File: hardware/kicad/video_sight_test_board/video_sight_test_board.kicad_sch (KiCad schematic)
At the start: 52 parts, among them J1 BATTERY, J2 XIAO_BREAKOUT_BOARD, J3 LCD, J4 BNO055_MODULE, J4 Conn_01x03_Pin, J5 ATtiny1616_LEFT, J6 ATtiny1616_RIGHT, J7 INPUT_DEVICE, Q1 AO3401A, SW1 SW_BATT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

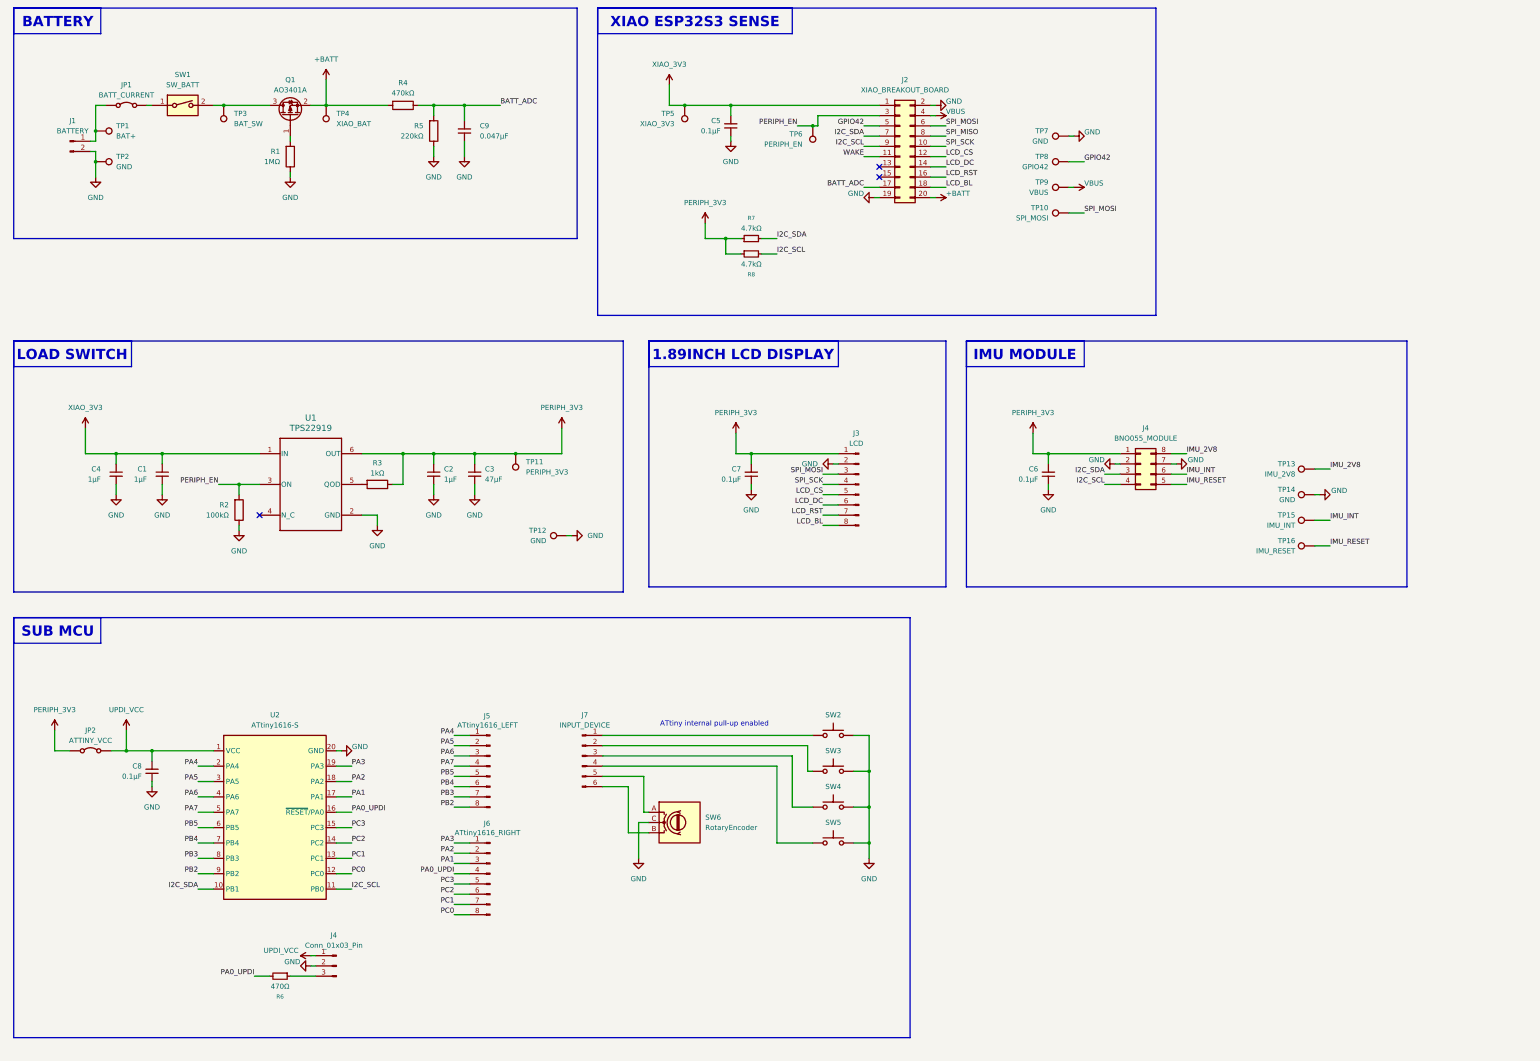
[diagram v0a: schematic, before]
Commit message: I2Cプルアップ注記追加
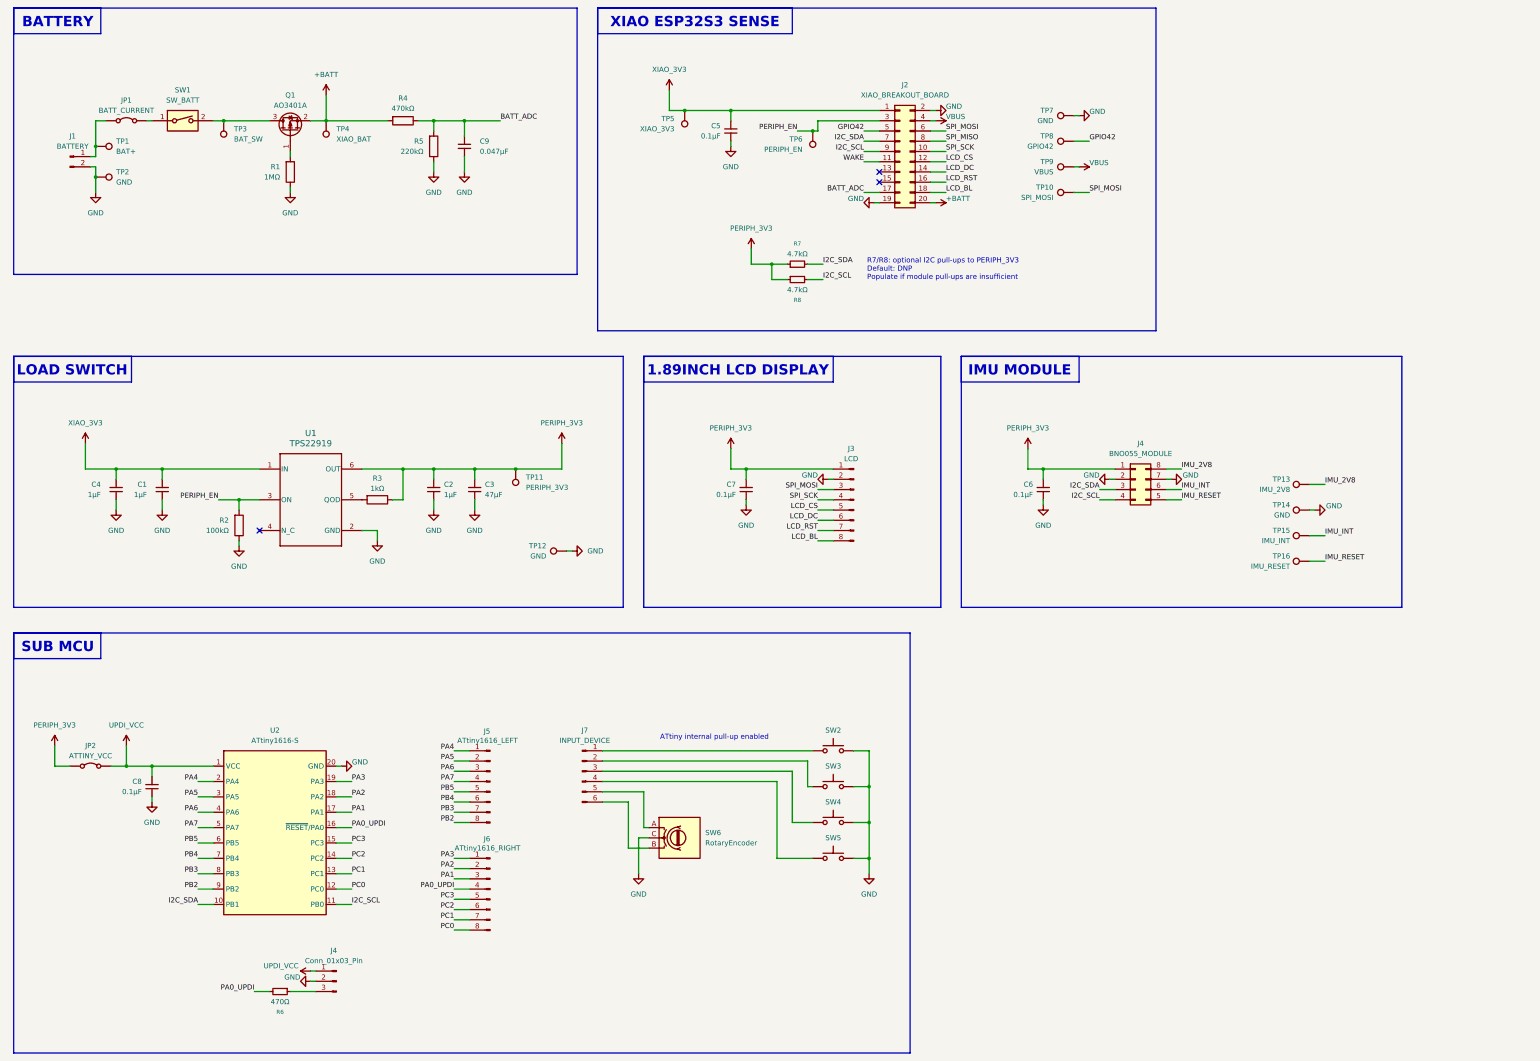
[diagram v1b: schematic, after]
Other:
- note added: "R7/R8: optional I2C pull-ups to PERIPH_3V3 Default: DNP Populate if module pull-ups are insufficient"
- moved on the sheet: C1, C2, C3, C4, C5, C6, C7, C8, C9, J1, J2, J3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

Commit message: フットプリント選定 微修正
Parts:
- C1, C2, C5, C6, C7, C8, C9: footprint (none) -> Capacitor_SMD:C_0805_2012Metric_Pad1.18x1.45mm_HandSolder
- C3: footprint (none) -> @自分用:CAP_FN_B_PAN
- C4: value 1μF -> 47μF; footprint (none) -> @自分用:CAP_FN_B_PAN
- J1: footprint (none) -> Connector_JST:JST_XH_B2B-XH-A_1x02_P2.50mm_Vertical
- J2: footprint (none) -> Connector_IDC:IDC-Header_2x10_P2.54mm_Vertical
- J3: footprint (none) -> Connector_PinHeader_2.54mm:PinHeader_1x08_P2.54mm_Vertical
- J4: footprint (none) -> Package_DIP:DIP-8_W7.62mm_Socket
- J5: renamed from J4; value Conn_01x03_Pin -> UPDI; footprint (none) -> Connector_PinHeader_2.54mm:PinHeader_1x03_P2.54mm_Vertical
- J6: renamed from J5; footprint (none) -> Connector_PinHeader_2.54mm:PinHeader_1x08_P2.54mm_Vertical
- J7: renamed from J6; footprint (none) -> Connector_PinHeader_2.54mm:PinHeader_1x08_P2.54mm_Vertical
- J8: renamed from J7; footprint (none) -> Connector_PinHeader_2.54mm:PinHeader_1x06_P2.54mm_Vertical
- JP1, JP2: footprint TestPoint:TestPoint_2Pads_Pitch2.54mm_Drill0.8mm -> Connector_PinHeader_2.54mm:PinHeader_1x02_P2.54mm_Vertical
- R1, R2, R3, R4, R5, R6: footprint (none) -> Resistor_SMD:R_0805_2012Metric_Pad1.20x1.40mm_HandSolder
- R7, R8: footprint (none) -> Resistor_SMD:R_0805_2012Metric_Pad1.20x1.40mm_HandSolder; now not fitted
- SW1: footprint (none) -> Button_Switch_THT:SW_DIP_SPSTx01_Slide_9.78x4.72mm_W7.62mm_P2.54mm
- SW2: value SW_MEC_5G -> UP; footprint (none) -> Button_Switch_THT:SW_PUSH_6mm; symbol Switch:SW_MEC_5G -> Switch:SW_Push
- SW3: value SW_MEC_5G -> DOWN; footprint (none) -> Button_Switch_THT:SW_PUSH_6mm; symbol Switch:SW_MEC_5G -> Switch:SW_Push
- SW4: value SW_MEC_5G -> FRONT; footprint (none) -> Button_Switch_THT:SW_PUSH_6mm; symbol Switch:SW_MEC_5G -> Switch:SW_Push
- SW5: value SW_MEC_5G -> BACK; footprint (none) -> Button_Switch_THT:SW_PUSH_6mm; symbol Switch:SW_MEC_5G -> Switch:SW_Push
- SW6: footprint (none) -> Rotary_Encoder:RotaryEncoder_Alps_EC12E_Vertical_H20mm
- TP1, TP10, TP11, TP12, TP14, TP15, TP16, TP2, TP3, TP4, TP5, TP6, TP7, TP8, TP9: footprint (none) -> TestPoint:TestPoint_THTPad_D1.5mm_Drill0.7mm
- TP13: value IMU_2V8 -> IMU_2V8_OUT; footprint (none) -> TestPoint:TestPoint_THTPad_D1.5mm_Drill0.7mm
- U1: footprint DCK0006A_N -> @自分用:DCK0006A_L
- U2: value ATtiny1616-S -> ATTINY1616-SN
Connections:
- net GND: now also SW2.2, SW3.2, SW4.2, SW5.2; no longer SW2.3 (B), SW2.4 (B), SW3.3 (B), SW3.4 (B), SW4.3 (B), SW4.4 (B), SW5.3 (B), SW5.4 (B)
- net at J8.4 (Pin_4), SW5.1: no longer SW5.2 (A)
- net at J8.1 (Pin_1), SW2.1: no longer SW2.2 (A)
- net at J8.2 (Pin_2), SW3.1: no longer SW3.2 (A)
- net at J8.3 (Pin_3), SW4.1: no longer SW4.2 (A)
- net IMU_2V8 renamed IMU_2V8_OUT

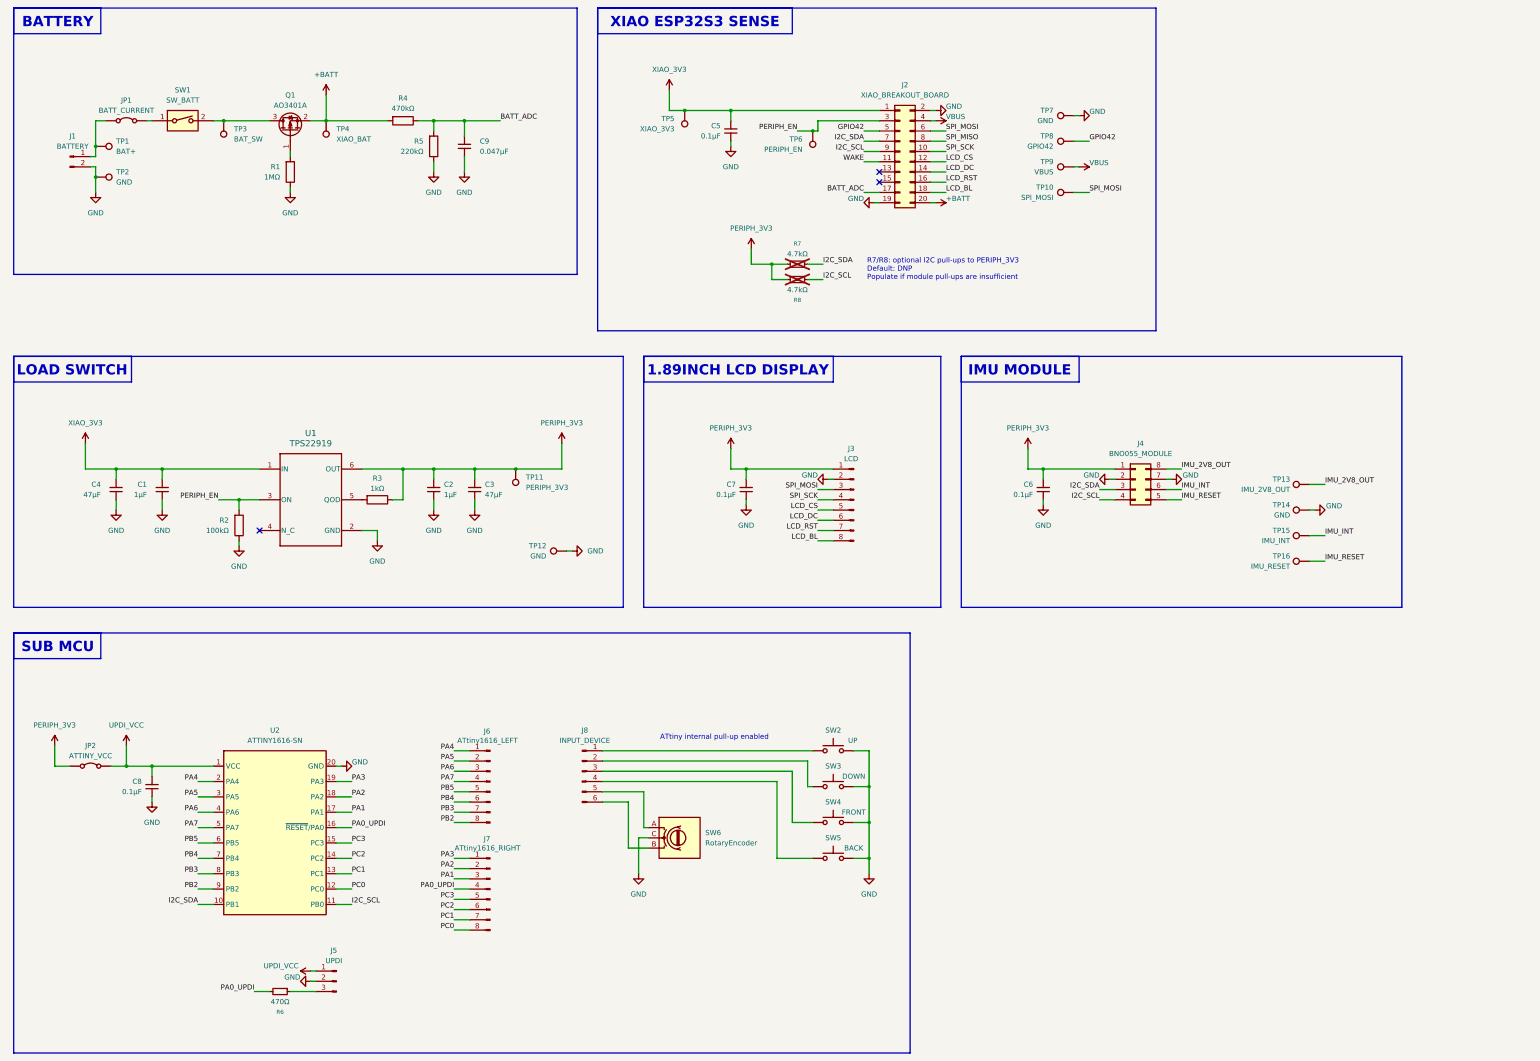
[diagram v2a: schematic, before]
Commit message: WAKEスイッチ追加 TP10修正
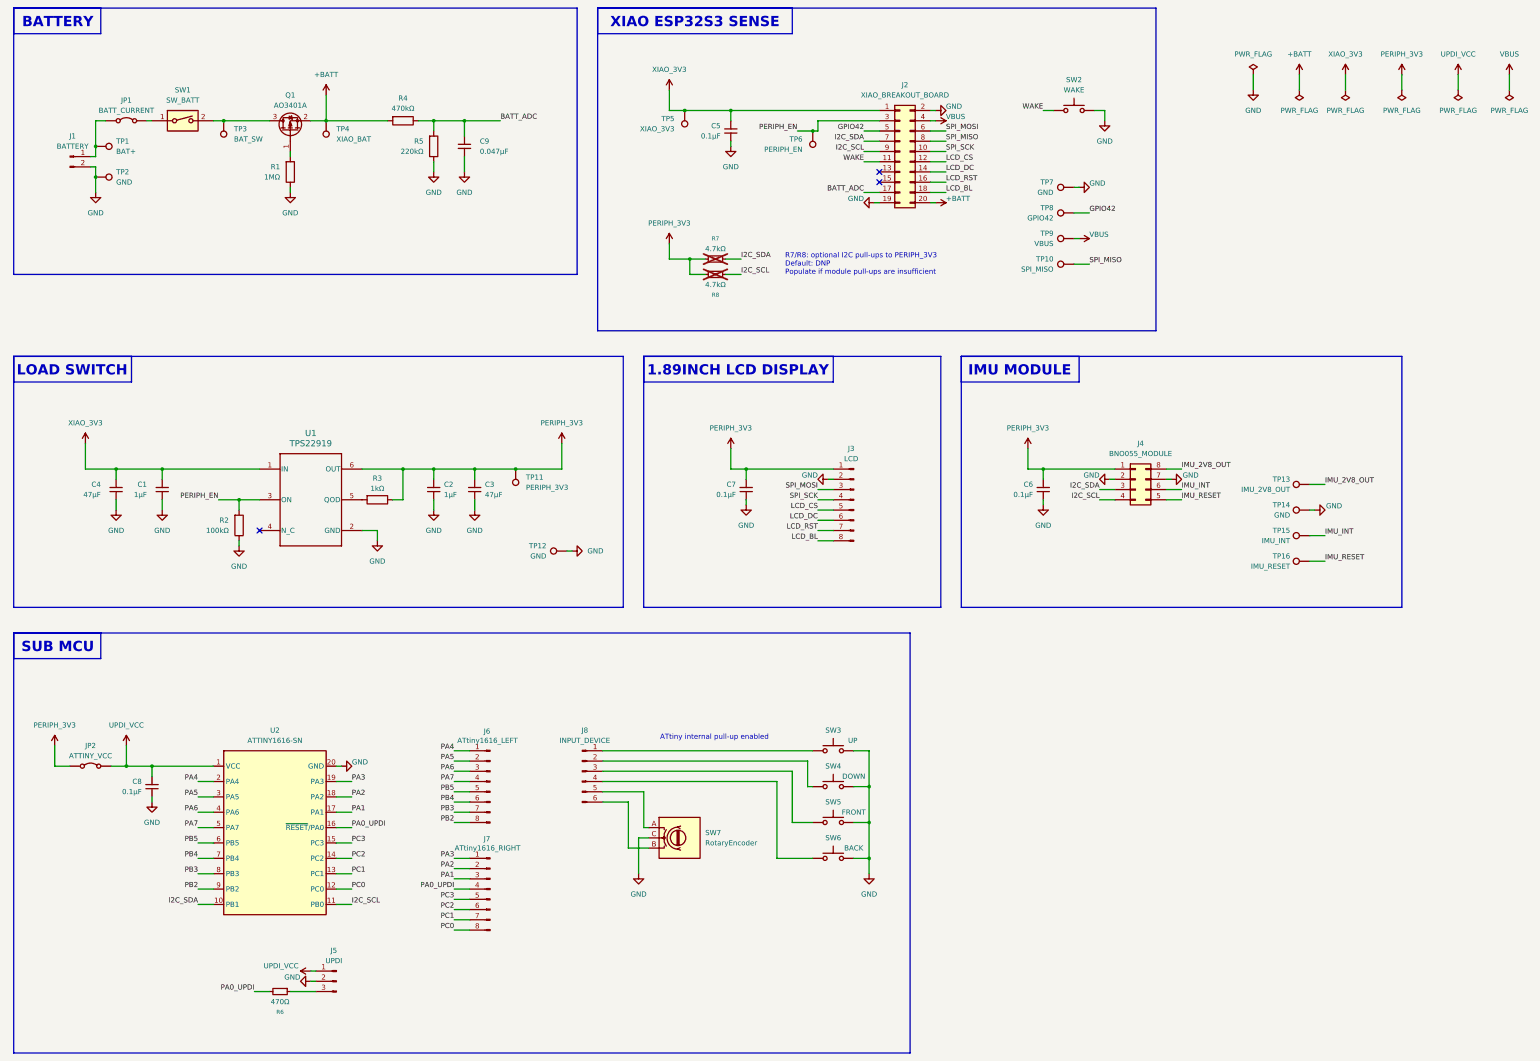
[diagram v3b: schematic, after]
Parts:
- added SW2: WAKE, Button_Switch_THT:SW_PUSH_6mm, symbol Switch:SW_Push
- TP10: value SPI_MOSI -> SPI_MISO
- renumbered SW2 to SW3, SW3 to SW4, SW4 to SW5, SW5 to SW6, SW6 to SW7
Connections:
- net GND: now also SW2.2
- net SPI_MISO: now also TP10.1
- net SPI_MOSI: no longer TP10.1
- net WAKE: now also SW2.1
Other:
- moved on the sheet: R7, R8, TP10, TP7, TP8, TP9

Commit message: PCBざっくり置いた
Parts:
- renumbered TP2 to TP1, TP1 to TP2
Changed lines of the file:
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@@
 		(dnp no)
 		(fields_autoplaced yes)
-		(property "Reference" "TP1"
+		(property "Reference" "TP2"
 			(at 41.91 49.5299 90)
 			(effects
@@
 			(project ""
 				(path "/1bc004cb-e275-41d9-96ac-81dd92544364"
-					(reference "TP1")
+					(reference "TP2")
 					(unit 1)
 				)
@@
 		(dnp no)
 		(fields_autoplaced yes)
-		(property "Reference" "TP2"
+		(property "Reference" "TP1"
 			(at 41.91 57.1499 90)
 			(effects
@@
 			(project "video_sight_test_board"
 				(path "/1bc004cb-e275-41d9-96ac-81dd92544364"
-					(reference "TP2")
+					(reference "TP1")
 					(unit 1)
 				)
